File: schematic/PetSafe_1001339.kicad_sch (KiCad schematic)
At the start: 150 parts, among them J1 ICSP, J3 PIR BOARD, J5 MOTOR, J6 DNP, Q1 FMOS3401A?, Q11 MMBTA55?, Q2 BC847B?, Q3 MMBTA55?, Q4 MMBTA55?, Q5 MMBTA55?, Q6 MMBTA55?, Q7 BC857C?, Q8 SIL3724A?, Q9 DNP, U1 S-1200B45?, U106 U6A / DNP, U2 SN74LVC2G14DBV?, U3 SGM8542XS, U4 PIC16F18855, U5 MX512H, U6 S-812C33AMC? / 3.3V, U7 DNP, Y1 20 MHz

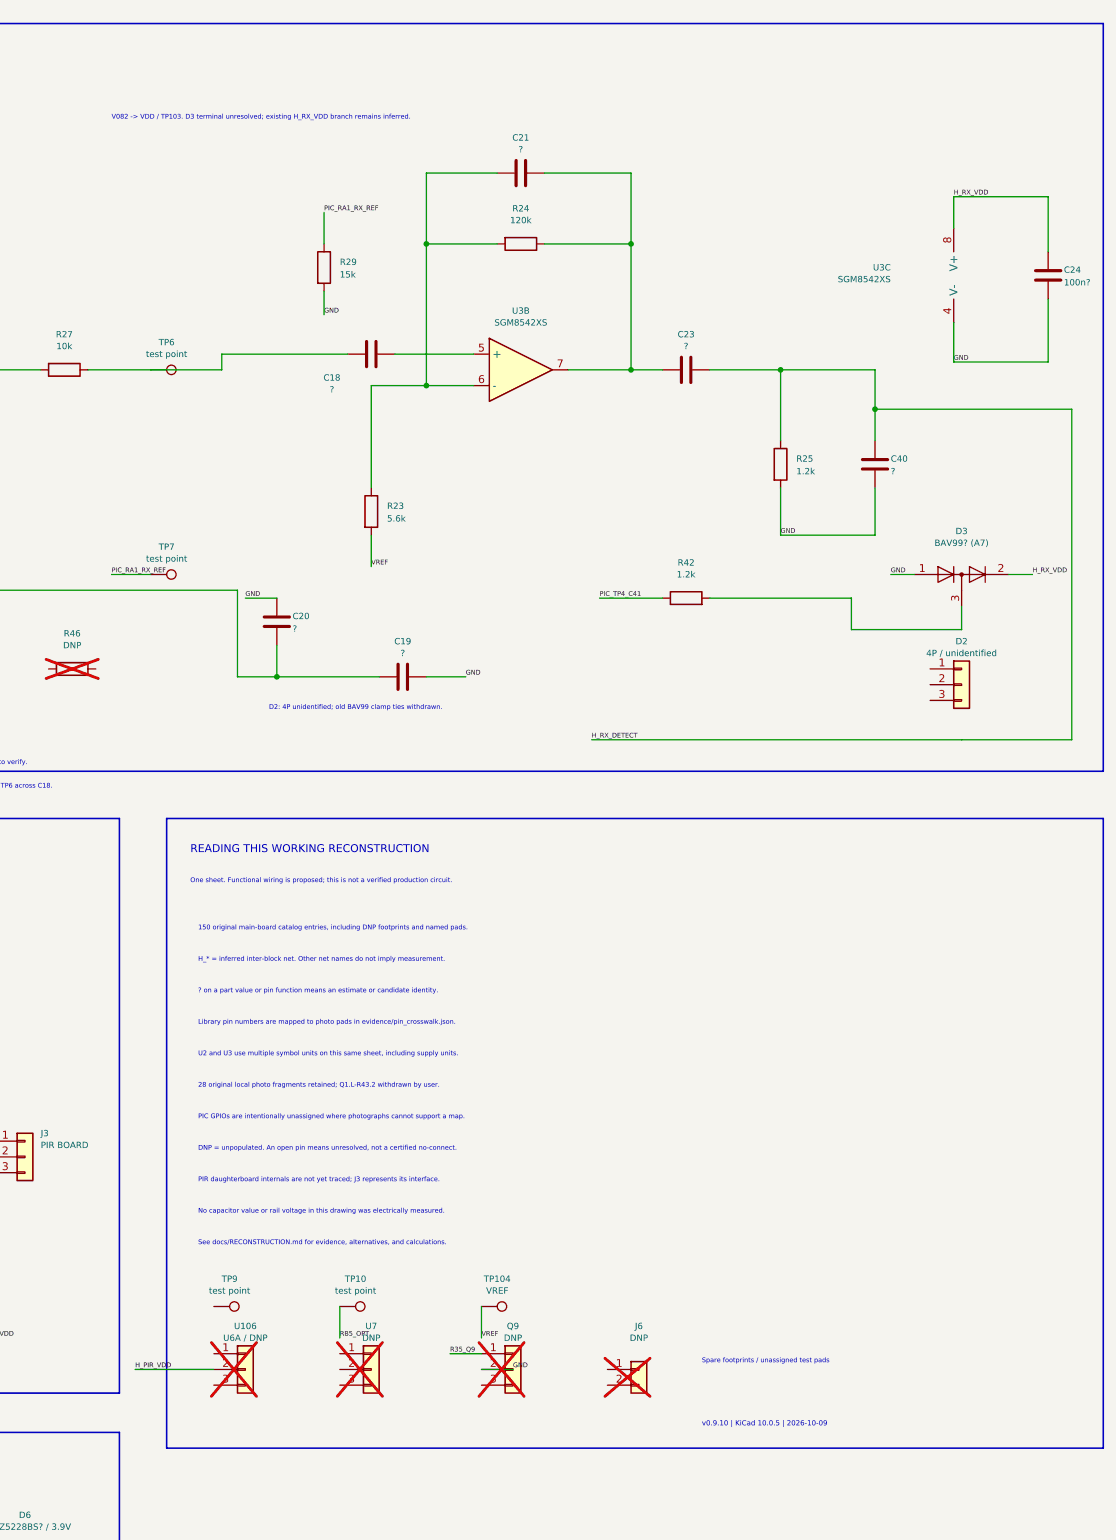
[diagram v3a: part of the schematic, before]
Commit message: Record measured D3 rails and R42 continuity; close V082 association
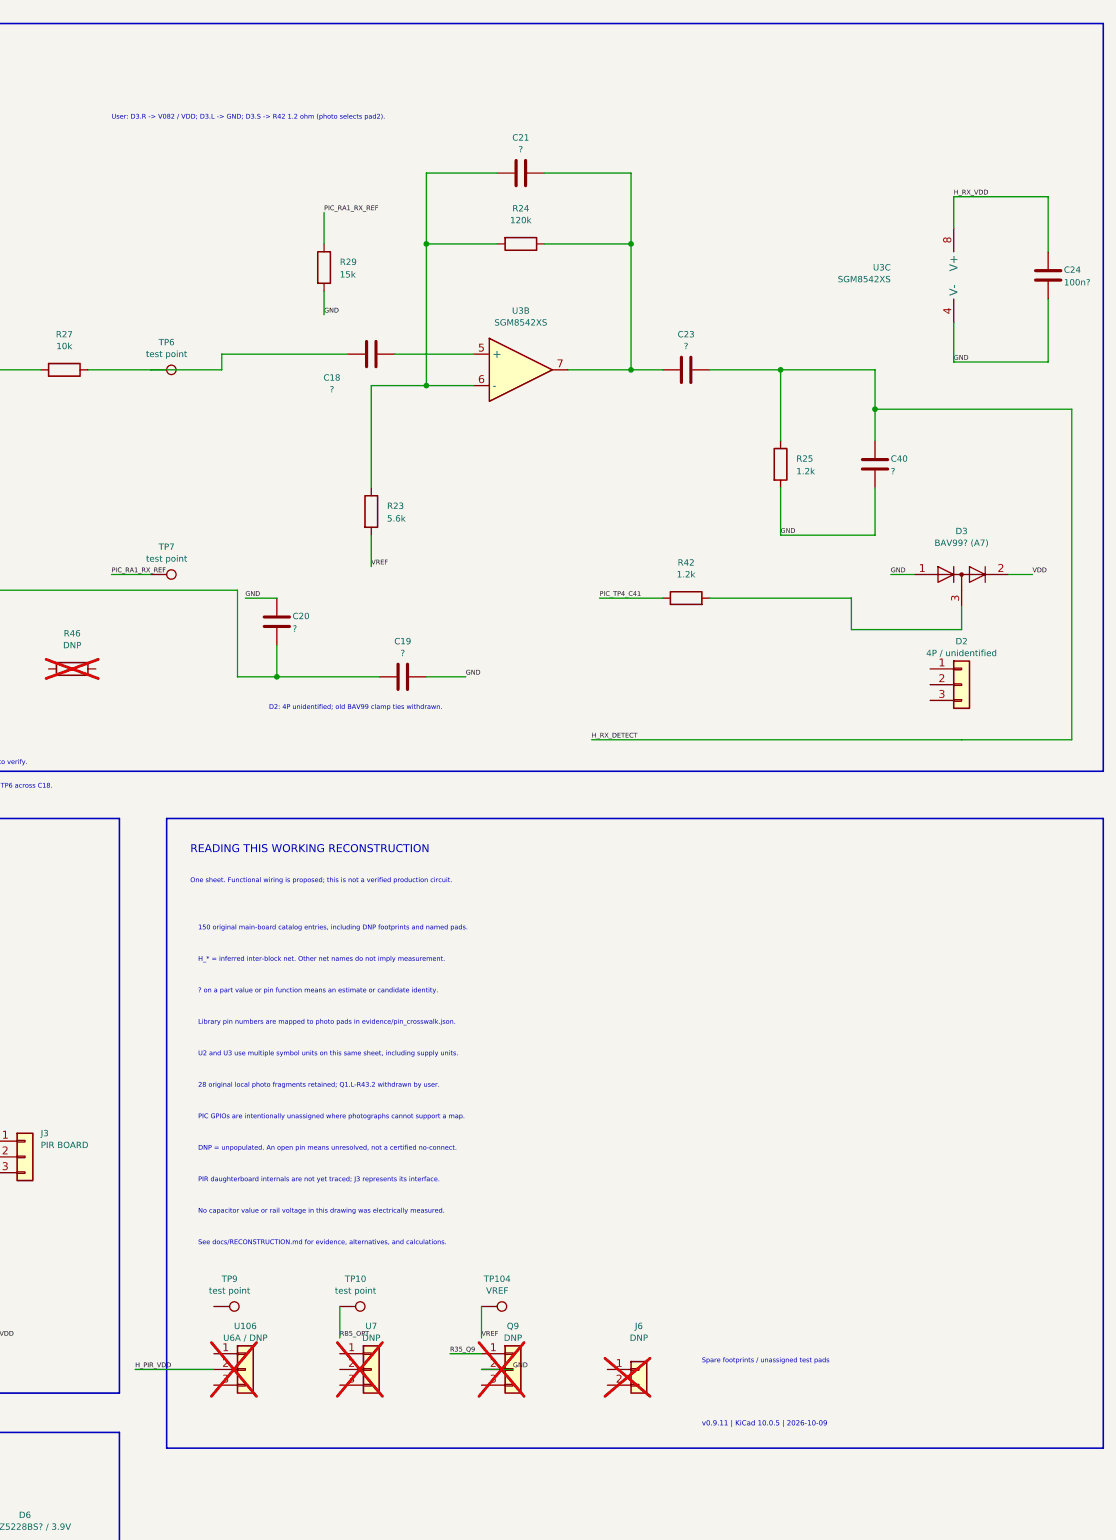
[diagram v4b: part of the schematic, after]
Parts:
- D3: PhysicalConnectionEvidence (none) -> 2026-10-09 user meter report: D3.L=GND; D3.R=VDD TP via V08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
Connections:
- net H_RX_VDD: no longer D3.2 (A)
- net VDD: now also D3.2 (A)
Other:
- note added: "User: D3.R -> V082 / VDD; D3.L -> GND; D3.S -> R42 1.2 ohm (photo selects pad2)."
- note added: "v0.9.11 | KiCad 10.0.5 | 2026-10-09"
- note removed: "V082 -> VDD / TP103. D3 terminal unresolved; existing H_RX_VDD branch remains inferred."
- note removed: "v0.9.10 | KiCad 10.0.5 | 2026-10-09"

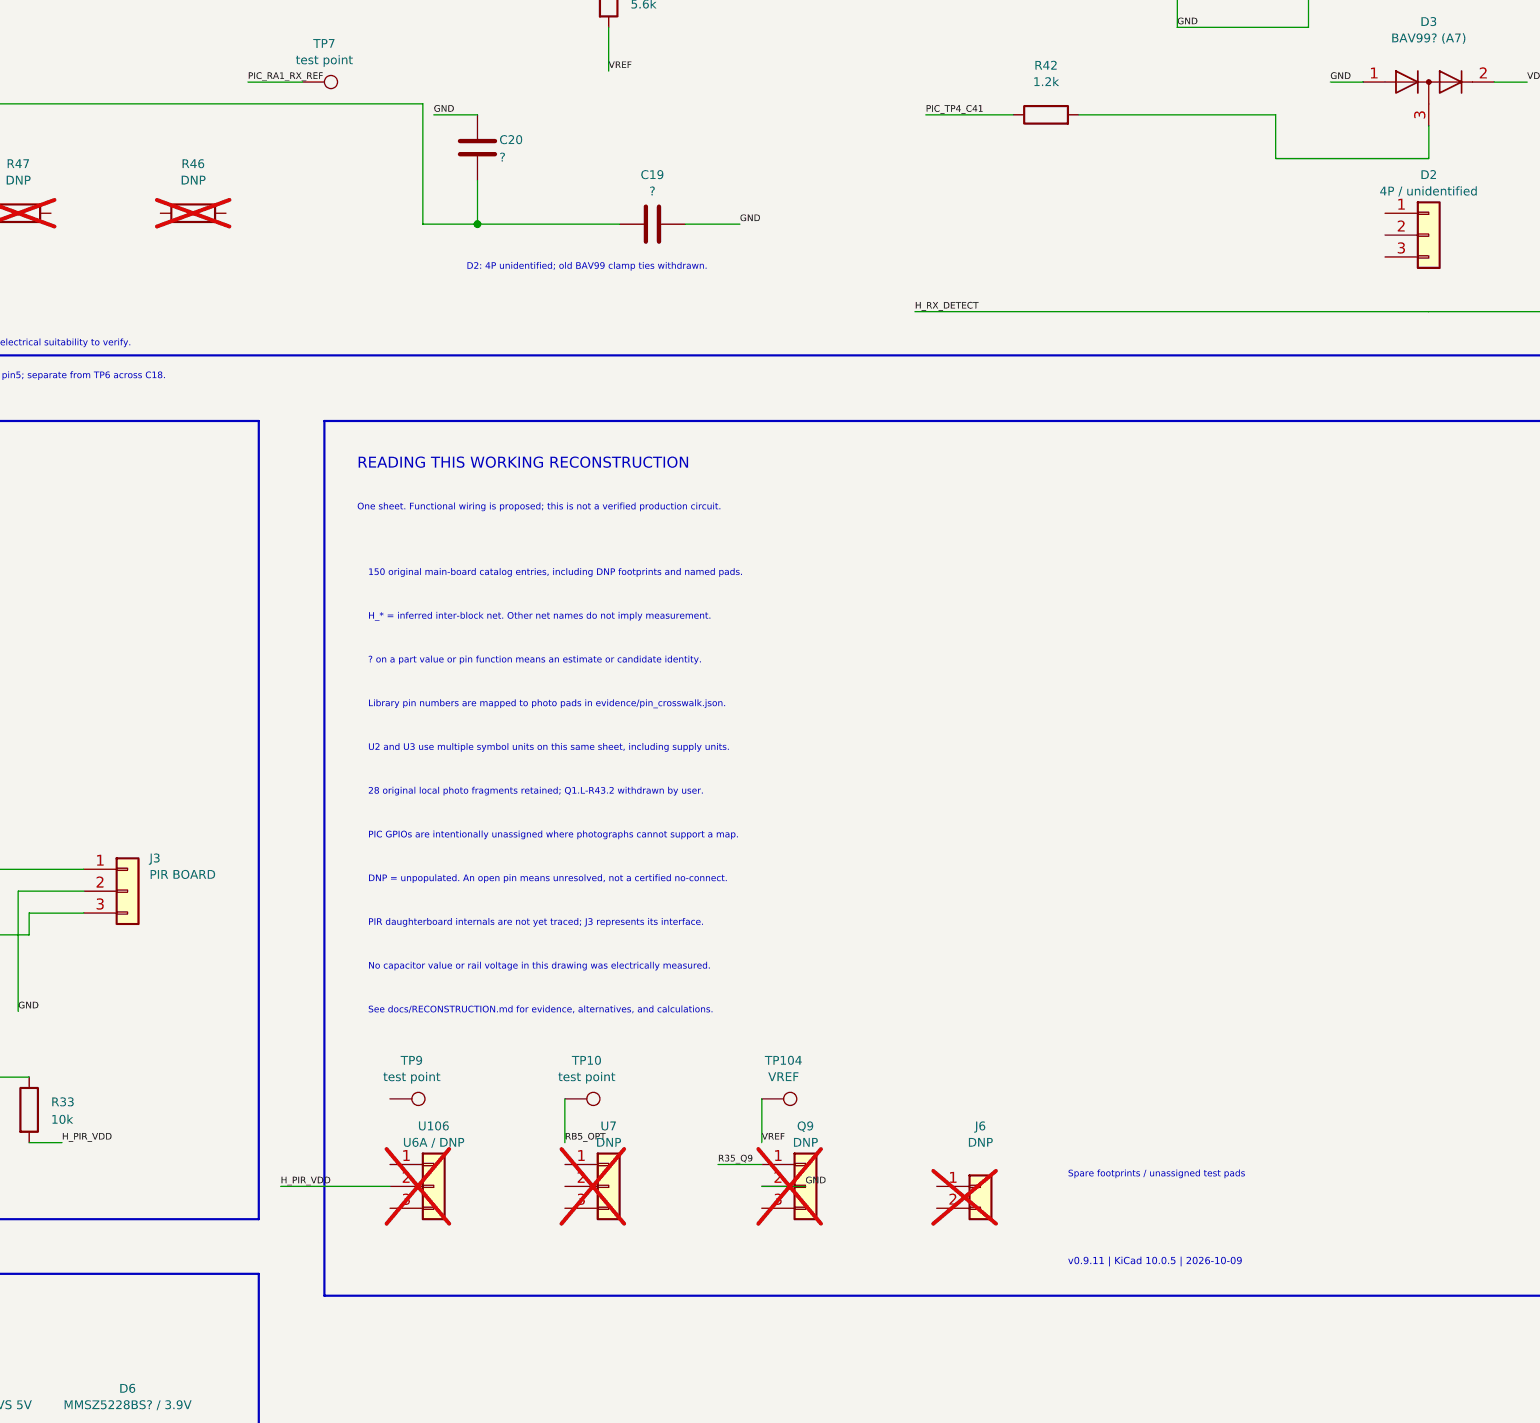
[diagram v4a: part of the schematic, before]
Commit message: Map D2 antenna and receiver connections with empty R46 option
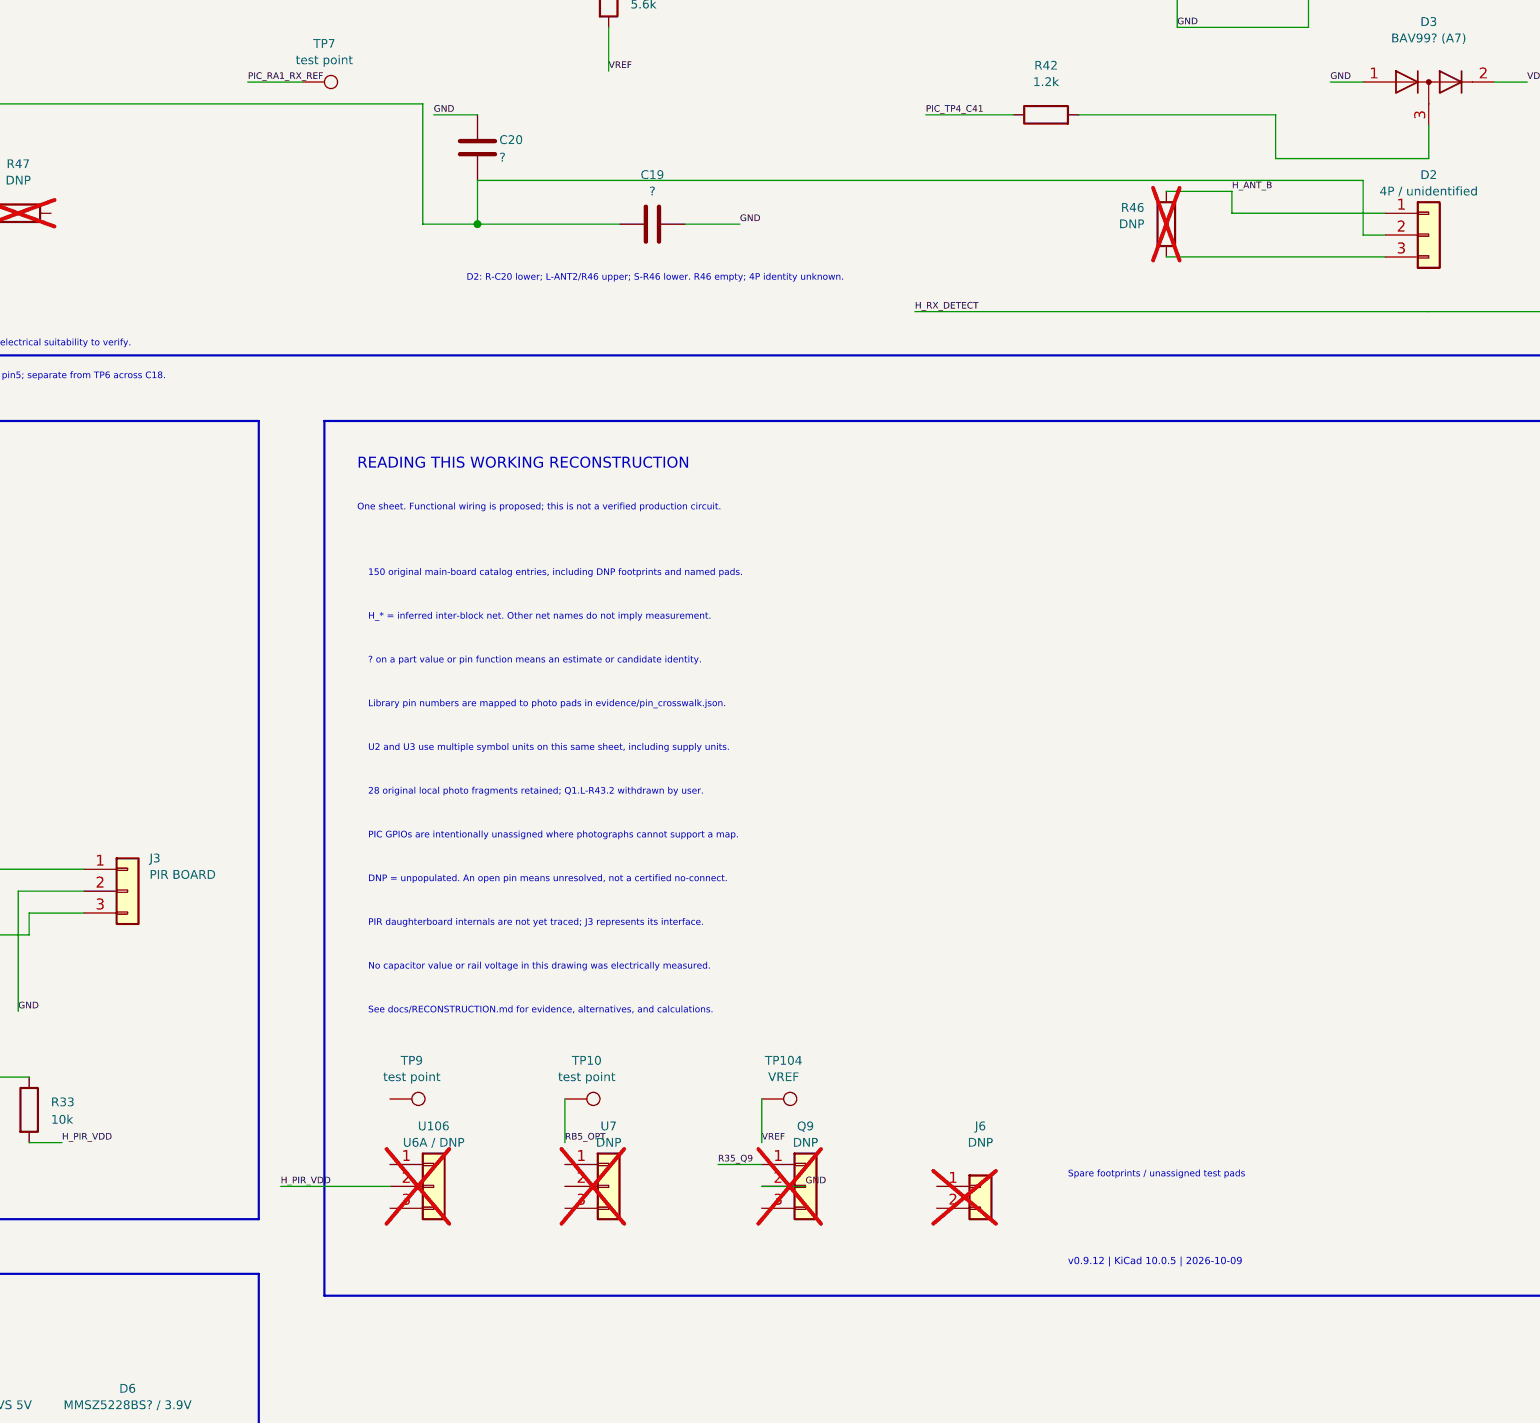
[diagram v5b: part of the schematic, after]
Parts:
- D2: MeasurementEvidence (none) -> User: R (upper-left)-C20 lower = 1 ohm; L (upper-right)-ANT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
- R46: MeasurementEvidence (none) -> User confirms empty R46 footprint: upper pad/model1 joins D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
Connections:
- net H_ANT_B: now also D2.1 (Pin_1), R46.1
- net at R46.2: now also D2.3 (Pin_3)
- net at C19.1, C20.2, R28.2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: now also D2.2 (Pin_2)
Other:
- note added: "D2: R-C20 lower; L-ANT2/R46 upper; S-R46 lower. R46 empty; 4P identity unknown."
- note added: "v0.9.12 | KiCad 10.0.5 | 2026-10-09"
- note removed: "D2: 4P unidentified; old BAV99 clamp ties withdrawn."
- note removed: "v0.9.11 | KiCad 10.0.5 | 2026-10-09"
- moved on the sheet: R46

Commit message: Resolve measured U3 bias and J3 ground; queue focused follow-up checks
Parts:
- J3: MeasurementEvidence (none) -> v0.9.13 user: pin3 (left / I in IMG_2435)-GND 1 ohm; pin2 (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; ViaEvidence v0.9.8: User confirms V067-J3 pin1 (red wire), on modeled H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 -> v0.9.13 user: pin3 (left / I in IMG_2435)-GND 1 ohm; pin2 (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
- R22: MeasurementEvidence (none) -> v0.9.13 user: D/left end in IMG_2434 is model2, U3.5/VREF a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; ViaEvidence v0.9.8: User confirms V071-VREF. Earlier V071-R21.2 and V02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 -> v0.9.13 user: D/left end in IMG_2434 is model2, U3.5/VREF a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
- R23: MeasurementEvidence (none) -> v0.9.13 user: both physical ends 270-289 kohm to U3.5, now 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; ViaEvidence v0.9.8: User confirms V071-VREF. Earlier V071-R21.2 and V02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 -> v0.9.13 user: both physical ends 270-289 kohm to U3.5, now 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
- U3: MeasurementEvidence (none) -> v0.9.13 user: pin5-VREF 1 ohm; pin5-R22 D/left 1 ohm, E/rig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
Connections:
- net GND: now also J3.3 (Pin_3); no longer J3.2 (Pin_2)
- net VREF: now also C18.1, U3.5 (+); no longer R23.2
- net at R33.1, R38.1: no longer J3.3 (Pin_3)
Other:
- note added: "User: U3 pin5 / V079 / V080 = VREF (1 ohm); TP6 remains separate across C18."
- note added: "v0.9.13 | KiCad 10.0.5 | 2026-10-09"
- note removed: "User: V072 = TP6, not R22.2. V079/V080 = U3 pin5; separate from TP6 across C18."
- note removed: "v0.9.12 | KiCad 10.0.5 | 2026-10-09"
